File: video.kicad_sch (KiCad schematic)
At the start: 55 parts, among them IC10 2318, IC11 MC14053, IC14 74LS86N, IC21 74LS123N, IC22 74LS00N, IC23 74ALS74N, IC27 74LS20N, IC28 74LS393N, IC29 74LS393N, IC30 74LS32N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

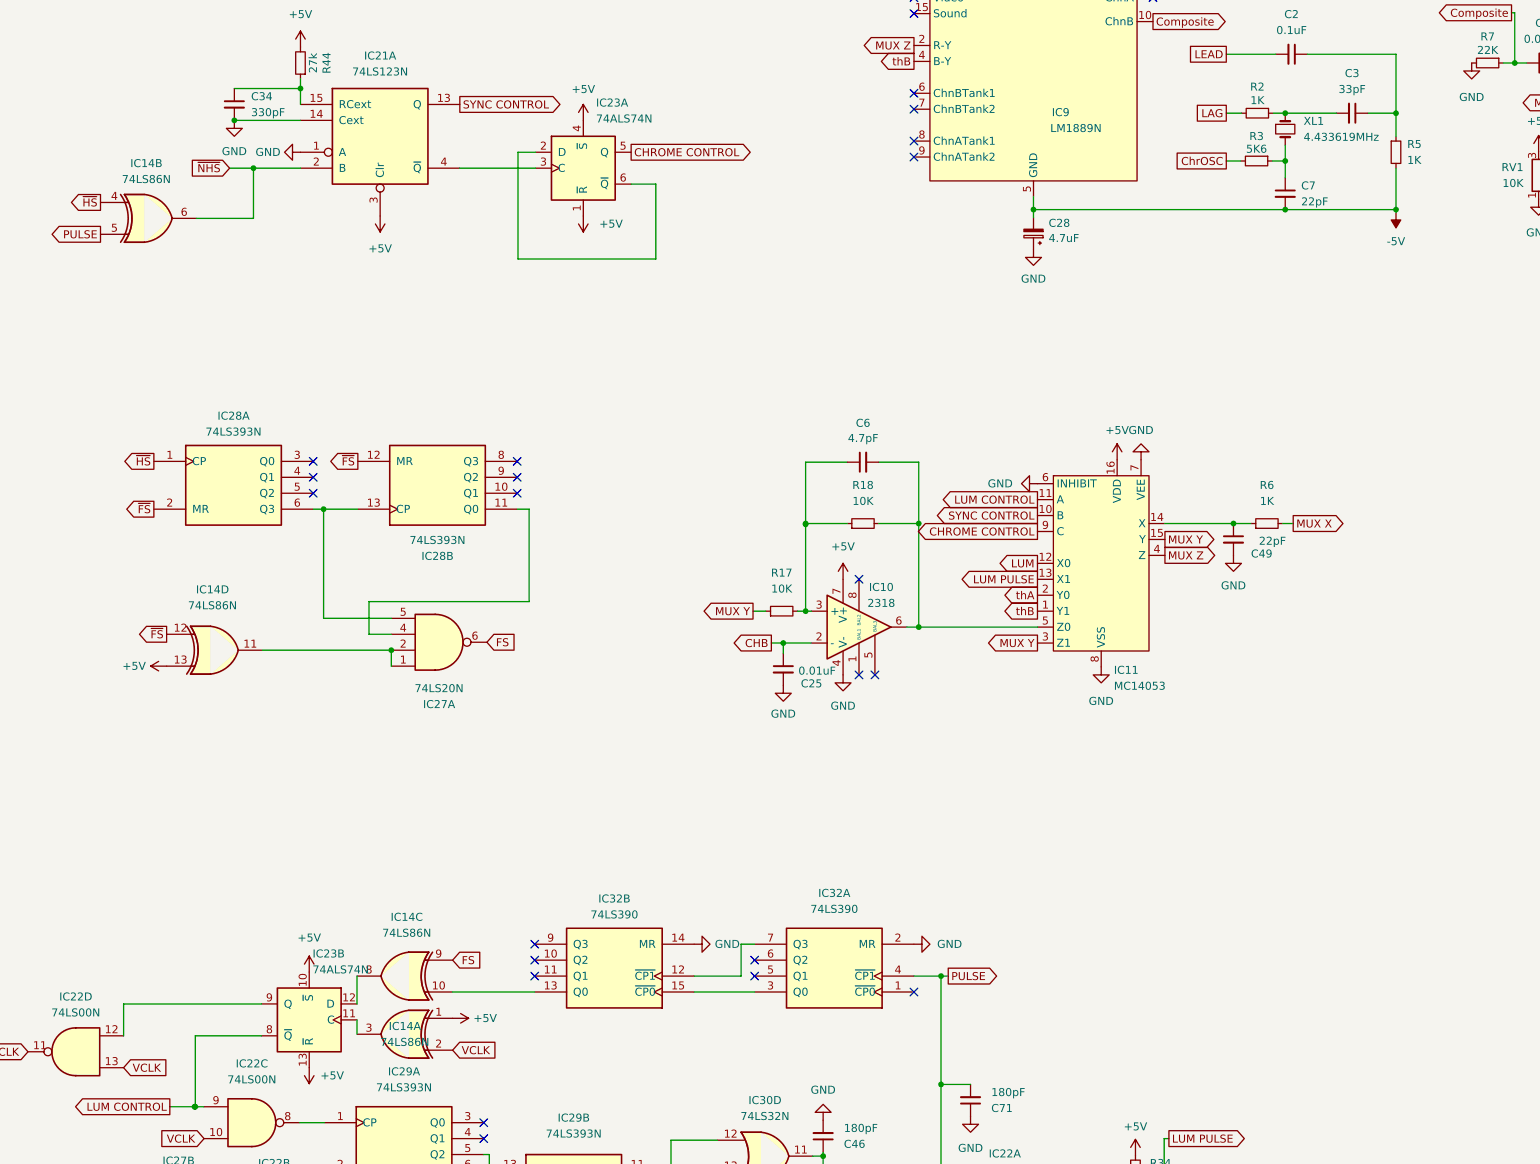
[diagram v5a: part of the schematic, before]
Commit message: update part numbers
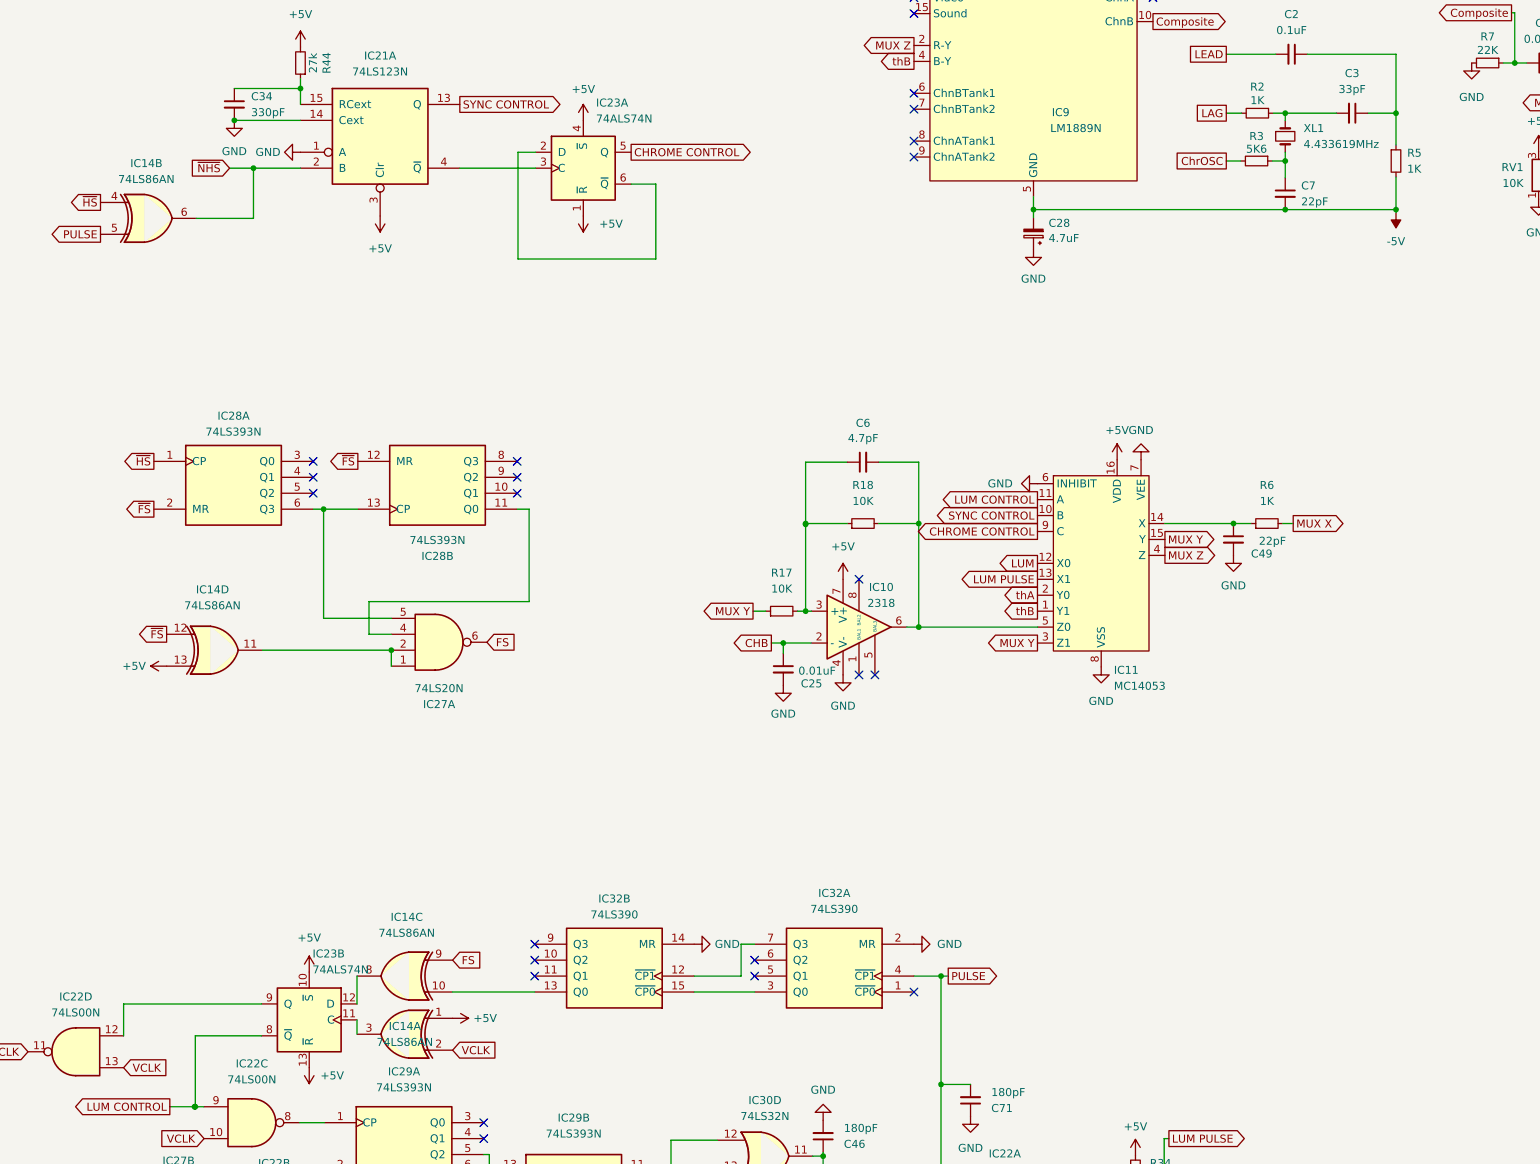
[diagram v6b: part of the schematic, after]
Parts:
- C2: DigiKey (none) -> BC1101CT-ND
- C25: DigiKey (none) -> BC2662CT-ND
- C3, C5: DigiKey (none) -> BC1007CT-ND
- C34: DigiKey (none) -> BC1045CT-ND
- C46, C71: DigiKey (none) -> BC1016CT-ND
- C47: DigiKey (none) -> 399-C316C101J5G5TA7303CT-ND
- C49, C7, C9: DigiKey (none) -> 399-13930-1-ND
- C6: DigiKey (none) -> 445-180473-1-ND
- C8: footprint Capacitor_THT:C_Disc_D4.7mm_W2.5mm_P5.00mm -> Capacitor_THT:C_Disc_D4.3mm_W1.9mm_P5.00mm; DigiKey (none) -> BC2662CT-ND
- IC10: Note (none) -> donor only
- IC11: DigiKey (none) -> 296-2059-ND; Note (none) -> obsolete use CD4053B
- IC14: value 74LS86N -> 74LS86AN; DigiKey (none) -> 296-1669-5-ND
- IC21: DigiKey (none) -> 296-1636-5-ND
- IC22: DigiKey (none) -> 296-1626-ND
- IC23: DigiKey (none) -> 296-1506-5-ND; Note (none) -> LS74 no longer produced, ALS or HCT instead
- IC23: DigiKey 296-1504-5-ND -> 296-1506-5-ND; Note (none) -> LS74 no longer produced, ALS or HCT instead
- IC27: DigiKey (none) -> 296-3670-5-ND
- IC28, IC29: DigiKey (none) -> 296-1665-5-ND
- IC30: DigiKey (none) -> 296-1658-5-ND
- IC32: DigiKey (none) -> 296-26516-5-ND
- IC9: Note (none) -> donor / NOS
- TR2, TR3: DigiKey (none) -> 2N4401D26ZCT-ND; Note (none) -> use 2N4401TFR
- TR4: DigiKey (none) -> 2N3906D26ZCT-ND; Note (none) -> use 2N3906
- XL1: footprint Crystal:Crystal_HC18-U_Horizontal -> Crystal:Crystal_HC49-U_Horizontal; DigiKey (none) -> 1923-830003099B-ND
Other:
- moved on the sheet: R5, XL1

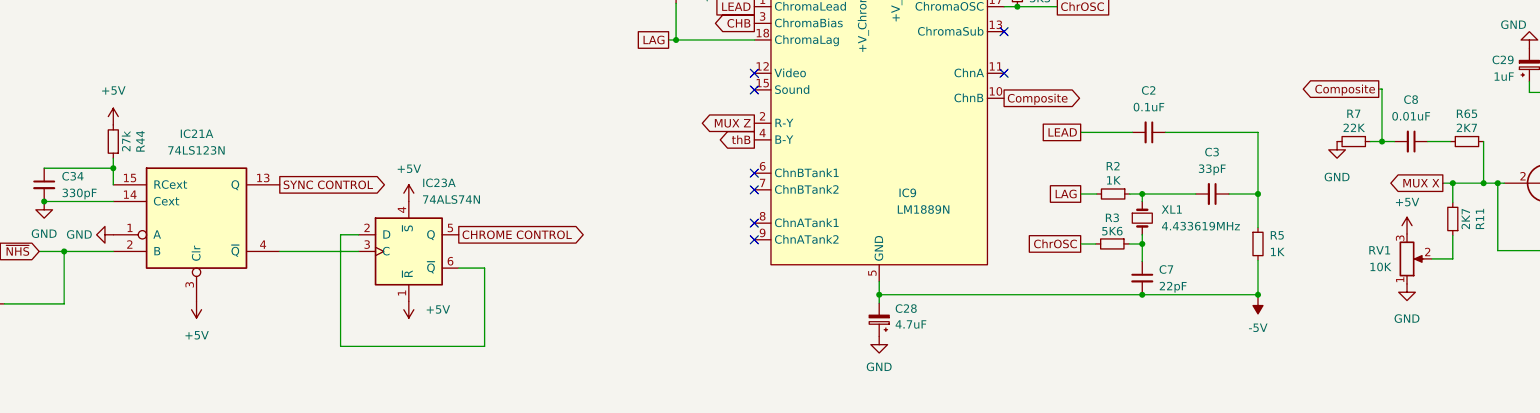
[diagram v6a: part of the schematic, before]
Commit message: resolve part numbers
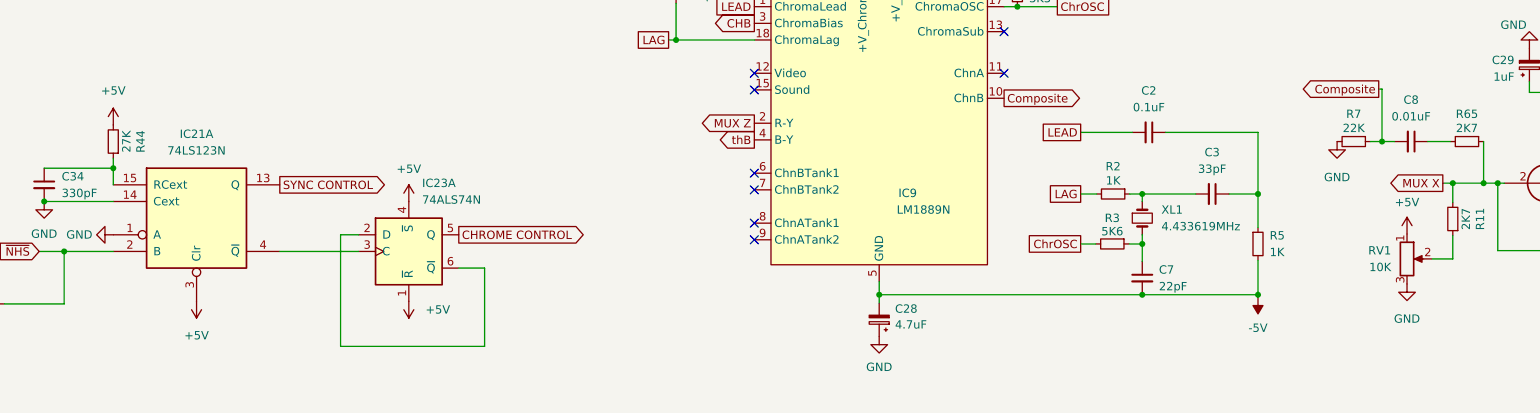
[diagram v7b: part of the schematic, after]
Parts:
- R10, R11, R65: DigiKey (none) -> CF14JT2K70CT-ND
- R17, R18: DigiKey (none) -> CF14JT10K0CT-ND
- R2, R5, R6: DigiKey (none) -> CF14JT1K00CT-ND
- R3, R68: DigiKey (none) -> CF14JT5K60CT-ND
- R33, R4: DigiKey (none) -> CF14JT3K30CT-ND
- R34: DigiKey (none) -> CF14JT6K80CT-ND
- R35: DigiKey (none) -> CF14JT15K0CT-ND
- R44: value 27k -> 27K; DigiKey (none) -> CF14JT27K0CT-ND
- R67: DigiKey (none) -> CF14JT1K20CT-ND
- R69: DigiKey (none) -> CF14JT330RCT-ND
- R7: DigiKey (none) -> CF14JT22K0CT-ND
- R76: DigiKey (none) -> CF14JT10R0CT-ND
- R8, R9: DigiKey (none) -> CF14JT270RCT-ND
- RV1: footprint Potentiometer_THT:Potentiometer_ACP_CA9-H5_Horizontal -> Potentiometer_THT:Potentiometer_Bourns_3386X_Horizontal; DigiKey (none) -> 3386H-103LF-ND
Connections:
- net +5V: now also RV1.1; no longer RV1.3
- net GND: now also RV1.3; no longer RV1.1
